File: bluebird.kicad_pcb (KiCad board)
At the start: 2 copper layers, 310.8 x 120.3 mm, 168 parts

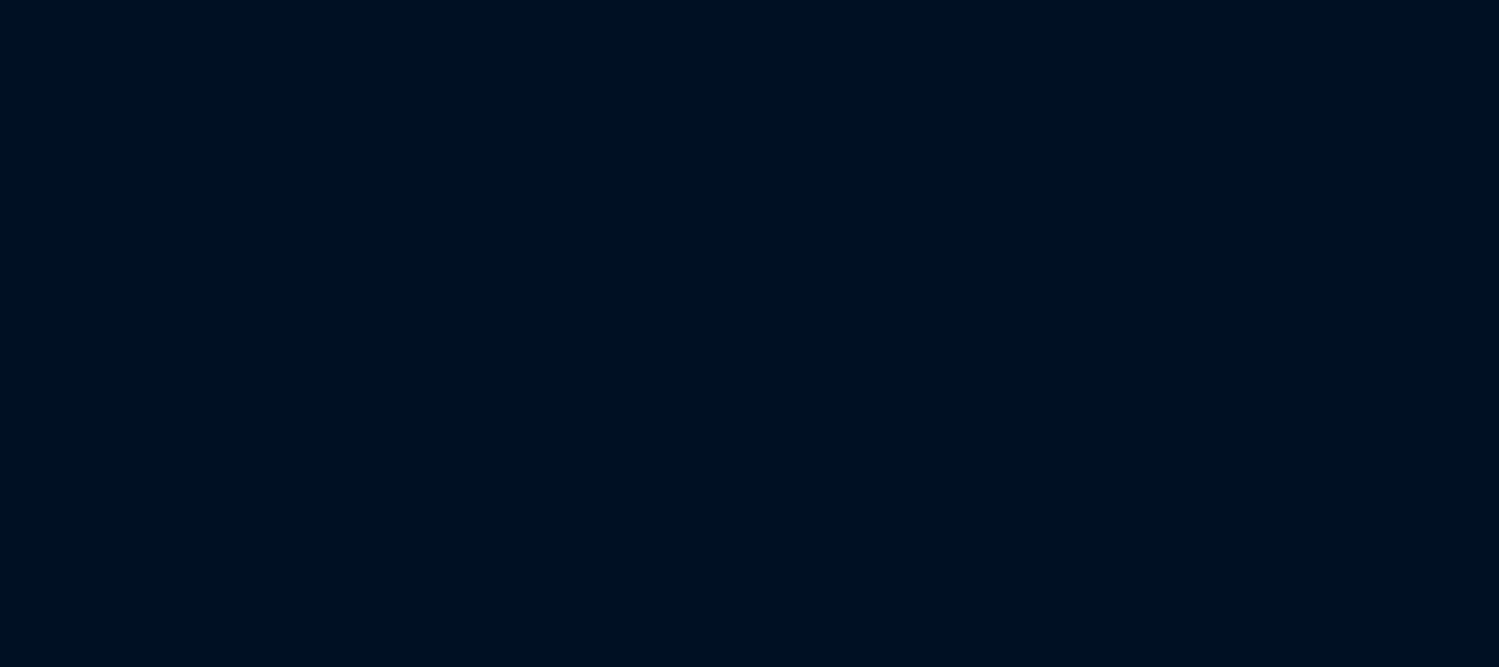
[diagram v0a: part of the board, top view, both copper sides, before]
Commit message: Add LED controller + LEDS
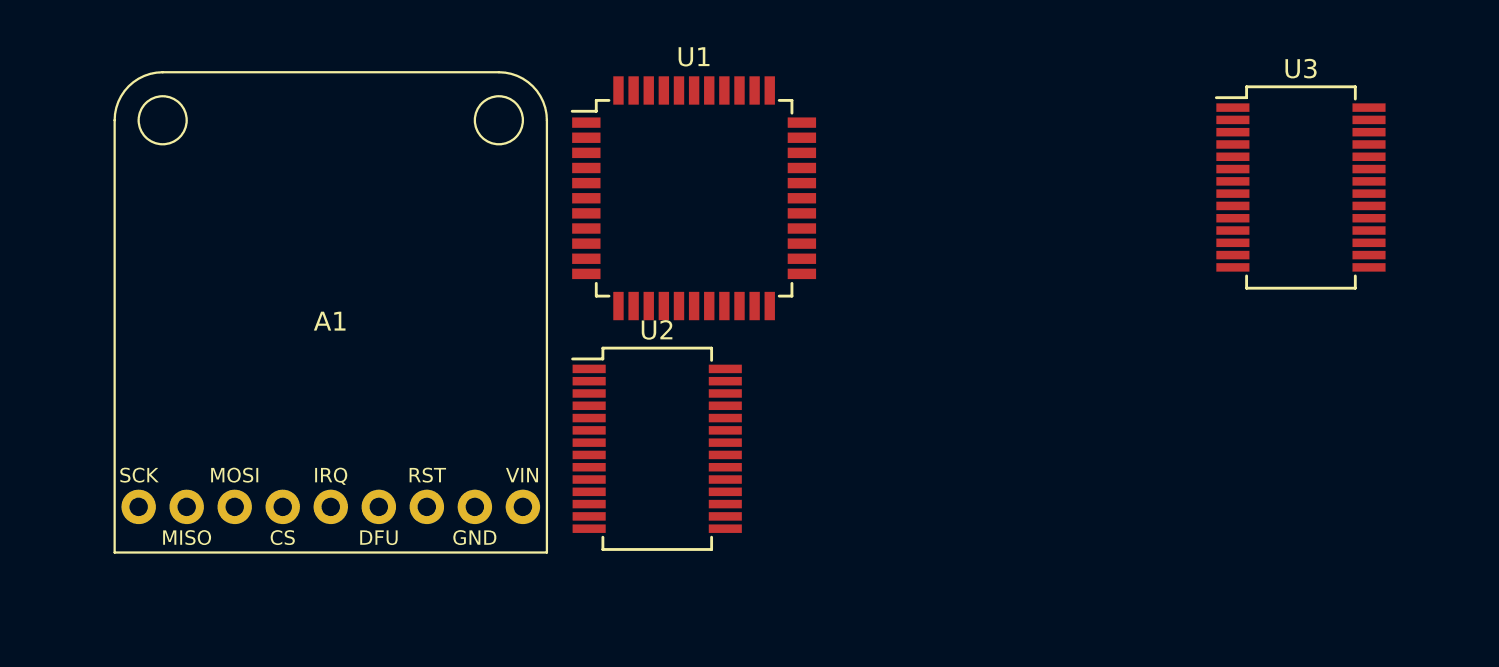
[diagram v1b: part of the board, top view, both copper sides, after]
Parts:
- added A1: BLUEFRUIT_SPI, bluebird:BLUEFRUIT_SPI_FRIEND, F.Cu at (179.8, 5.59)
- added U1: ATMEGA32U4, Package_QFP:TQFP-44_10x10mm_P0.8mm, F.Cu at (199.0, -13.1)
- added U2: MCP23017_SS, Package_SO:SSOP-28_5.3x10.2mm_P0.65mm, F.Cu at (197.1, 0.10)
- added U3: IS31FL3731-SA, Package_SO:SSOP-28_5.3x10.2mm_P0.65mm, F.Cu at (231.1, -13.7)
- K_0_0, K_1_0, K_2_0, K_3_0, K_4_0, K_5_0, K_6_0, K_7_0, K_8_0, K_9_0, K_ALT1_0, K_A_0, K_B_0, K_COMMA_0, K_CTRL1_0, K_C_0, K_DOT_0, K_DOWN_0, K_D_0, K_END_0, K_EQUAL_0, K_ESC_0, K_E_0, K_F10_0, K_F11_0, K_F12_0, K_F1_0, K_F2_0, K_F3_0, K_F4_0, K_F5_0, K_F6_0, K_F7_0, K_F8_0, K_F9_0, K_FN_0, K_F_0, K_G_0, K_HOME_0, K_H_0, K_INSERT_0, K_I_0, K_J_0, K_K_0, K_LEFT_0, K_L_0, K_MINUS_0, K_M_0, K_NMLK_0, K_N_0, K_O_0, K_PAGE_DOWN_0, K_PAGE_UP_0, K_P_0, K_QUOTE_0, K_Q_0, K_RIGHT_0, K_R_0, K_SCRLK_0, K_SEMIC_0, K_SLASH_0, K_S_0, K_T_0, K_UP_0, K_U_0, K_V_0, K_W_0, K_X_0, K_Y_0, K_Z_0, K_[_0, K_]_0, K_`_0: footprint MX_Alps_Hybrid:MX-1U-NoLED -> MX_Alps_Hybrid:MX-1U
- K_ALT_0, K_CTRL_0, K_WIN_0: footprint MX_Alps_Hybrid:MX-1.25U-NoLED -> MX_Alps_Hybrid:MX-1.25U
- K_BACKSPACE_0: footprint MX_Alps_Hybrid:MX-2U-NoLED -> MX_Alps_Hybrid:MX-2U
- K_BSLSH_0, K_TAB_0: footprint MX_Alps_Hybrid:MX-1.5U-NoLED -> MX_Alps_Hybrid:MX-1.5U
- K_CAPS_LOCK_0, K_SHIFT1_0: footprint MX_Alps_Hybrid:MX-1.75U-NoLED -> MX_Alps_Hybrid:MX-1.75U
- K_ENTER_0, K_SHIFT_0: footprint MX_Alps_Hybrid:MX-2.25U-NoLED -> MX_Alps_Hybrid:MX-2.25U
- K_SPC_0: footprint MX_Alps_Hybrid:MX-6.25U-NoLED -> MX_Alps_Hybrid:MX-6.25U
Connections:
- K_0_0 pad 3: (no net) -> Net-(K_0_0-Pad3)
- K_0_0 pad 4: (no net) -> Net-(K_0_0-Pad4)
- K_1_0 pad 3: (no net) -> Net-(K_1_0-Pad3)
- K_1_0 pad 4: (no net) -> Net-(K_1_0-Pad4)
- K_2_0 pad 3: (no net) -> Net-(K_2_0-Pad3)
- K_2_0 pad 4: (no net) -> Net-(K_2_0-Pad4)
- K_3_0 pad 3: (no net) -> Net-(K_3_0-Pad3)
- K_3_0 pad 4: (no net) -> Net-(K_3_0-Pad4)
- K_4_0 pad 3: (no net) -> Net-(K_4_0-Pad3)
- K_4_0 pad 4: (no net) -> Net-(K_4_0-Pad4)
- K_5_0 pad 3: (no net) -> Net-(K_5_0-Pad3)
- K_5_0 pad 4: (no net) -> Net-(K_5_0-Pad4)
- K_6_0 pad 3: (no net) -> Net-(K_6_0-Pad3)
- K_6_0 pad 4: (no net) -> Net-(K_6_0-Pad4)
- K_7_0 pad 3: (no net) -> Net-(K_7_0-Pad3)
- K_7_0 pad 4: (no net) -> Net-(K_7_0-Pad4)
- K_8_0 pad 3: (no net) -> Net-(K_8_0-Pad3)
- K_8_0 pad 4: (no net) -> Net-(K_8_0-Pad4)
- K_9_0 pad 3: (no net) -> Net-(K_9_0-Pad3)
- K_9_0 pad 4: (no net) -> Net-(K_9_0-Pad4)
- K_ALT1_0 pad 3: (no net) -> Net-(K_ALT1_0-Pad3)
- K_ALT1_0 pad 4: (no net) -> Net-(K_ALT1_0-Pad4)
- K_ALT_0 pad 3: (no net) -> Net-(K_ALT_0-Pad3)
- K_ALT_0 pad 4: (no net) -> Net-(K_ALT_0-Pad4)
- K_A_0 pad 3: (no net) -> Net-(K_A_0-Pad3)
- K_A_0 pad 4: (no net) -> Net-(K_A_0-Pad4)
- K_BACKSPACE_0 pad 3: (no net) -> Net-(K_BACKSPACE_0-Pad3)
- K_BACKSPACE_0 pad 4: (no net) -> Net-(K_BACKSPACE_0-Pad4)
- K_BSLSH_0 pad 3: (no net) -> Net-(K_BSLSH_0-Pad3)
- K_BSLSH_0 pad 4: (no net) -> Net-(K_BSLSH_0-Pad4)
- K_B_0 pad 3: (no net) -> Net-(K_B_0-Pad3)
- K_B_0 pad 4: (no net) -> Net-(K_B_0-Pad4)
- K_CAPS_LOCK_0 pad 3: (no net) -> Net-(K_CAPS_LOCK_0-Pad3)
- K_CAPS_LOCK_0 pad 4: (no net) -> Net-(K_CAPS_LOCK_0-Pad4)
- K_COMMA_0 pad 3: (no net) -> Net-(K_COMMA_0-Pad3)
- K_COMMA_0 pad 4: (no net) -> Net-(K_COMMA_0-Pad4)
- K_CTRL1_0 pad 3: (no net) -> Net-(K_CTRL1_0-Pad3)
- K_CTRL1_0 pad 4: (no net) -> Net-(K_CTRL1_0-Pad4)
- K_CTRL_0 pad 3: (no net) -> Net-(K_CTRL_0-Pad3)
- K_CTRL_0 pad 4: (no net) -> Net-(K_CTRL_0-Pad4)
- K_C_0 pad 3: (no net) -> Net-(K_C_0-Pad3)
- K_C_0 pad 4: (no net) -> Net-(K_C_0-Pad4)
- K_DOT_0 pad 3: (no net) -> Net-(K_DOT_0-Pad3)
- K_DOT_0 pad 4: (no net) -> Net-(K_DOT_0-Pad4)
- K_DOWN_0 pad 3: (no net) -> Net-(K_DOWN_0-Pad3)
- K_DOWN_0 pad 4: (no net) -> Net-(K_DOWN_0-Pad4)
- K_D_0 pad 3: (no net) -> Net-(K_D_0-Pad3)
- K_D_0 pad 4: (no net) -> Net-(K_D_0-Pad4)
- K_END_0 pad 3: (no net) -> Net-(K_END_0-Pad3)
- K_END_0 pad 4: (no net) -> Net-(K_END_0-Pad4)
- K_ENTER_0 pad 3: (no net) -> Net-(K_ENTER_0-Pad3)
- K_ENTER_0 pad 4: (no net) -> Net-(K_ENTER_0-Pad4)
- K_EQUAL_0 pad 3: (no net) -> Net-(K_EQUAL_0-Pad3)
- K_EQUAL_0 pad 4: (no net) -> Net-(K_EQUAL_0-Pad4)
- K_ESC_0 pad 3: (no net) -> Net-(K_ESC_0-Pad3)
- K_ESC_0 pad 4: (no net) -> Net-(K_ESC_0-Pad4)
- K_E_0 pad 3: (no net) -> Net-(K_E_0-Pad3)
- K_E_0 pad 4: (no net) -> Net-(K_E_0-Pad4)
- K_F10_0 pad 3: (no net) -> Net-(K_F10_0-Pad3)
- K_F10_0 pad 4: (no net) -> Net-(K_F10_0-Pad4)
- K_F11_0 pad 3: (no net) -> Net-(K_F11_0-Pad3)
- K_F11_0 pad 4: (no net) -> Net-(K_F11_0-Pad4)
- K_F12_0 pad 3: (no net) -> Net-(K_F12_0-Pad3)
- K_F12_0 pad 4: (no net) -> Net-(K_F12_0-Pad4)
- K_F1_0 pad 3: (no net) -> Net-(K_F1_0-Pad3)
- K_F1_0 pad 4: (no net) -> Net-(K_F1_0-Pad4)
- K_F2_0 pad 3: (no net) -> Net-(K_F2_0-Pad3)
- K_F2_0 pad 4: (no net) -> Net-(K_F2_0-Pad4)
- K_F3_0 pad 3: (no net) -> Net-(K_F3_0-Pad3)
- K_F3_0 pad 4: (no net) -> Net-(K_F3_0-Pad4)
- K_F4_0 pad 3: (no net) -> Net-(K_F4_0-Pad3)
- K_F4_0 pad 4: (no net) -> Net-(K_F4_0-Pad4)
- K_F5_0 pad 3: (no net) -> Net-(K_F5_0-Pad3)
- K_F5_0 pad 4: (no net) -> Net-(K_F5_0-Pad4)
- K_F6_0 pad 3: (no net) -> Net-(K_F6_0-Pad3)
- K_F6_0 pad 4: (no net) -> Net-(K_F6_0-Pad4)
- K_F7_0 pad 3: (no net) -> Net-(K_F7_0-Pad3)
- K_F7_0 pad 4: (no net) -> Net-(K_F7_0-Pad4)
- K_F8_0 pad 3: (no net) -> Net-(K_F8_0-Pad3)
- K_F8_0 pad 4: (no net) -> Net-(K_F8_0-Pad4)
- K_F9_0 pad 3: (no net) -> Net-(K_F9_0-Pad3)
- K_F9_0 pad 4: (no net) -> Net-(K_F9_0-Pad4)
- K_FN_0 pad 3: (no net) -> Net-(K_FN_0-Pad3)
- K_FN_0 pad 4: (no net) -> Net-(K_FN_0-Pad4)
- K_F_0 pad 3: (no net) -> Net-(K_F_0-Pad3)
- K_F_0 pad 4: (no net) -> Net-(K_F_0-Pad4)
- K_G_0 pad 3: (no net) -> Net-(K_G_0-Pad3)
- K_G_0 pad 4: (no net) -> Net-(K_G_0-Pad4)
- K_HOME_0 pad 3: (no net) -> Net-(K_HOME_0-Pad3)
- K_HOME_0 pad 4: (no net) -> Net-(K_HOME_0-Pad4)
- K_H_0 pad 3: (no net) -> Net-(K_H_0-Pad3)
- K_H_0 pad 4: (no net) -> Net-(K_H_0-Pad4)
- K_INSERT_0 pad 3: (no net) -> Net-(K_INSERT_0-Pad3)
- K_INSERT_0 pad 4: (no net) -> Net-(K_INSERT_0-Pad4)
- K_I_0 pad 3: (no net) -> Net-(K_I_0-Pad3)
- K_I_0 pad 4: (no net) -> Net-(K_I_0-Pad4)
- K_J_0 pad 3: (no net) -> Net-(K_J_0-Pad3)
- K_J_0 pad 4: (no net) -> Net-(K_J_0-Pad4)
- K_K_0 pad 3: (no net) -> Net-(K_K_0-Pad3)
- K_K_0 pad 4: (no net) -> Net-(K_K_0-Pad4)
- K_LEFT_0 pad 3: (no net) -> Net-(K_LEFT_0-Pad3)
- K_LEFT_0 pad 4: (no net) -> Net-(K_LEFT_0-Pad4)
- K_L_0 pad 3: (no net) -> Net-(K_L_0-Pad3)
- K_L_0 pad 4: (no net) -> Net-(K_L_0-Pad4)
- K_MINUS_0 pad 3: (no net) -> Net-(K_MINUS_0-Pad3)
- K_MINUS_0 pad 4: (no net) -> Net-(K_MINUS_0-Pad4)
- K_M_0 pad 3: (no net) -> Net-(K_M_0-Pad3)
- K_M_0 pad 4: (no net) -> Net-(K_M_0-Pad4)
- K_NMLK_0 pad 3: (no net) -> Net-(K_NMLK_0-Pad3)
- K_NMLK_0 pad 4: (no net) -> Net-(K_NMLK_0-Pad4)
- K_N_0 pad 3: (no net) -> Net-(K_N_0-Pad3)
- K_N_0 pad 4: (no net) -> Net-(K_N_0-Pad4)
- K_O_0 pad 3: (no net) -> Net-(K_O_0-Pad3)
- K_O_0 pad 4: (no net) -> Net-(K_O_0-Pad4)
- K_PAGE_DOWN_0 pad 3: (no net) -> Net-(K_PAGE_DOWN_0-Pad3)
- K_PAGE_DOWN_0 pad 4: (no net) -> Net-(K_PAGE_DOWN_0-Pad4)
- K_PAGE_UP_0 pad 3: (no net) -> Net-(K_PAGE_UP_0-Pad3)
- K_PAGE_UP_0 pad 4: (no net) -> Net-(K_PAGE_UP_0-Pad4)
- K_P_0 pad 3: (no net) -> Net-(K_P_0-Pad3)
- K_P_0 pad 4: (no net) -> Net-(K_P_0-Pad4)
- K_QUOTE_0 pad 3: (no net) -> Net-(K_QUOTE_0-Pad3)
- K_QUOTE_0 pad 4: (no net) -> Net-(K_QUOTE_0-Pad4)
- K_Q_0 pad 3: (no net) -> Net-(K_Q_0-Pad3)
- K_Q_0 pad 4: (no net) -> Net-(K_Q_0-Pad4)
- K_RIGHT_0 pad 3: (no net) -> Net-(K_RIGHT_0-Pad3)
- K_RIGHT_0 pad 4: (no net) -> Net-(K_RIGHT_0-Pad4)
- K_R_0 pad 3: (no net) -> Net-(K_R_0-Pad3)
- K_R_0 pad 4: (no net) -> Net-(K_R_0-Pad4)
- K_SCRLK_0 pad 3: (no net) -> Net-(K_SCRLK_0-Pad3)
- K_SCRLK_0 pad 4: (no net) -> Net-(K_SCRLK_0-Pad4)
- K_SEMIC_0 pad 3: (no net) -> Net-(K_SEMIC_0-Pad3)
- K_SEMIC_0 pad 4: (no net) -> Net-(K_SEMIC_0-Pad4)
- K_SHIFT1_0 pad 3: (no net) -> Net-(K_SHIFT1_0-Pad3)
- K_SHIFT1_0 pad 4: (no net) -> Net-(K_SHIFT1_0-Pad4)
- K_SHIFT_0 pad 3: (no net) -> Net-(K_SHIFT_0-Pad3)
- K_SHIFT_0 pad 4: (no net) -> Net-(K_SHIFT_0-Pad4)
- K_SLASH_0 pad 3: (no net) -> Net-(K_SLASH_0-Pad3)
- K_SLASH_0 pad 4: (no net) -> Net-(K_SLASH_0-Pad4)
- K_SPC_0 pad 3: (no net) -> Net-(K_SPC_0-Pad3)
- K_SPC_0 pad 4: (no net) -> Net-(K_SPC_0-Pad4)
- K_S_0 pad 3: (no net) -> Net-(K_S_0-Pad3)
- K_S_0 pad 4: (no net) -> Net-(K_S_0-Pad4)
- K_TAB_0 pad 3: (no net) -> Net-(K_TAB_0-Pad3)
- K_TAB_0 pad 4: (no net) -> Net-(K_TAB_0-Pad4)
- K_T_0 pad 3: (no net) -> Net-(K_T_0-Pad3)
- K_T_0 pad 4: (no net) -> Net-(K_T_0-Pad4)
- K_UP_0 pad 3: (no net) -> Net-(K_UP_0-Pad3)
- K_UP_0 pad 4: (no net) -> Net-(K_UP_0-Pad4)
- K_U_0 pad 3: (no net) -> Net-(K_U_0-Pad3)
- K_U_0 pad 4: (no net) -> Net-(K_U_0-Pad4)
- K_V_0 pad 3: (no net) -> Net-(K_V_0-Pad3)
- K_V_0 pad 4: (no net) -> Net-(K_V_0-Pad4)
- K_WIN_0 pad 3: (no net) -> Net-(K_WIN_0-Pad3)
- K_WIN_0 pad 4: (no net) -> Net-(K_WIN_0-Pad4)
- K_W_0 pad 3: (no net) -> Net-(K_W_0-Pad3)
- K_W_0 pad 4: (no net) -> Net-(K_W_0-Pad4)
- K_X_0 pad 3: (no net) -> Net-(K_X_0-Pad3)
- K_X_0 pad 4: (no net) -> Net-(K_X_0-Pad4)
- K_Y_0 pad 3: (no net) -> Net-(K_Y_0-Pad3)
- K_Y_0 pad 4: (no net) -> Net-(K_Y_0-Pad4)
- K_Z_0 pad 3: (no net) -> Net-(K_Z_0-Pad3)
- K_Z_0 pad 4: (no net) -> Net-(K_Z_0-Pad4)
- K_[_0 pad 3: (no net) -> Net-(K_[_0-Pad3)
- K_[_0 pad 4: (no net) -> Net-(K_[_0-Pad4)
- K_]_0 pad 3: (no net) -> Net-(K_]_0-Pad3)
- K_]_0 pad 4: (no net) -> Net-(K_]_0-Pad4)
- K_`_0 pad 3: (no net) -> Net-(K_`_0-Pad3)
- K_`_0 pad 4: (no net) -> Net-(K_`_0-Pad4)

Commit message: Finish charge controller, finish layout
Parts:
- added C1: 0.1u, Capacitor_SMD:C_0805_2012Metric_Pad1.15x1.40mm_HandSolder, B.Cu at (199.1, 144.1)
- added C10: 0.1u, Capacitor_SMD:C_0805_2012Metric_Pad1.15x1.40mm_HandSolder, B.Cu at (180.0, 136.6)
- added C11: 1u, Capacitor_SMD:C_0805_2012Metric_Pad1.15x1.40mm_HandSolder, B.Cu at (171.3, 147.7)
- added C12: 0.1u, Capacitor_SMD:C_0805_2012Metric_Pad1.15x1.40mm_HandSolder, B.Cu at (171.3, 149.7)
- added C13: 22uF, Capacitor_SMD:C_0805_2012Metric_Pad1.15x1.40mm_HandSolder, B.Cu at (132.6, 33.3)
- added C14: 22uF, Capacitor_SMD:C_0805_2012Metric_Pad1.15x1.40mm_HandSolder, B.Cu at (130.6, 33.3)
- added C15: 4.7u, Capacitor_SMD:C_0805_2012Metric_Pad1.15x1.40mm_HandSolder, B.Cu at (94.4, 34.4)
- added C2: 0.1u, Capacitor_SMD:C_0805_2012Metric_Pad1.15x1.40mm_HandSolder, B.Cu at (182.1, 141.9)
- added C3: 0.1u, Capacitor_SMD:C_0805_2012Metric_Pad1.15x1.40mm_HandSolder, B.Cu at (186.3, 130.2)
- added C4: 0.1u, Capacitor_SMD:C_0805_2012Metric_Pad1.15x1.40mm_HandSolder, B.Cu at (200.0, 134.6)
- added C5: 4.7u, Capacitor_SMD:C_0805_2012Metric_Pad1.15x1.40mm_HandSolder, B.Cu at (195.3, 147.0)
- added C6: 22p, Capacitor_SMD:C_0805_2012Metric_Pad1.15x1.40mm_HandSolder, B.Cu at (204.7, 146.2)
- added C7: 22p, Capacitor_SMD:C_0805_2012Metric_Pad1.15x1.40mm_HandSolder, B.Cu at (204.2, 136.0)
- added C8: 1u, Capacitor_SMD:C_0805_2012Metric_Pad1.15x1.40mm_HandSolder, B.Cu at (190.5, 146.9)
- added C9: 0.22u, Capacitor_SMD:C_0805_2012Metric_Pad1.15x1.40mm_HandSolder, B.Cu at (166.4, 144.2)
- added D1: B340, Diode_SMD:D_SMC, B.Cu at (163.5, 31.1)
- added D2: B340, Diode_SMD:D_SMC, B.Cu at (152.4, 31.1)
- added D3: LED_BLUE, LED_SMD:LED_0805_2012Metric, B.Cu at (97.5, 28.6)
- added D4: LED_RED, LED_SMD:LED_0805_2012Metric, B.Cu at (140.8, 31.4)
- added J1: USB_C_Receptacle_USB2.0, Connector_USB:USB_C_Receptacle_GCT_USB4085, B.Cu at (46.7, 32.4)
- added J2: Conn_01x02_Male, Connector_JST:JST_PH_S2B-PH-K_1x02_P2.00mm_Horizontal, B.Cu at (104.6, 30.9)
- added J3: Conn_01x07, Connector_PinHeader_2.54mm:PinHeader_1x07_P2.54mm_Vertical, B.Cu at (148.0, 148.0)
- added JP1: SolderJumper_3_Bridged12, Connector_PinHeader_2.54mm:PinHeader_1x03_P2.54mm_Vertical, B.Cu at (90.1, 30.9)
- added L1: 2.2u 3A, Inductor_SMD:L_Vishay_IHLP-1212, B.Cu at (118.3, 33.1)
- added R1: 10k, Resistor_SMD:R_0805_2012Metric_Pad1.15x1.40mm_HandSolder, B.Cu at (197.8, 150.1)
- added R10: 750k, Resistor_SMD:R_0805_2012Metric_Pad1.15x1.40mm_HandSolder, B.Cu at (134.7, 31.3)
- added R11: 100k, Resistor_SMD:R_0805_2012Metric_Pad1.15x1.40mm_HandSolder, B.Cu at (137.6, 30.3)
- added R12: 1k, Resistor_SMD:R_0805_2012Metric_Pad1.15x1.40mm_HandSolder, B.Cu at (99.5, 28.6)
- added R13: 2k, Resistor_SMD:R_0805_2012Metric_Pad1.15x1.40mm_HandSolder, B.Cu at (86.9, 30.1)
- added R14: 10k, Resistor_SMD:R_0805_2012Metric_Pad1.15x1.40mm_HandSolder, B.Cu at (86.9, 32.2)
- added R15: 4.7k, Resistor_SMD:R_0805_2012Metric_Pad1.15x1.40mm_HandSolder, B.Cu at (143.8, 30.3)
- added R2: 22R, Resistor_SMD:R_0805_2012Metric_Pad1.15x1.40mm_HandSolder, B.Cu at (190.5, 151.1)
- added R3: 22R, Resistor_SMD:R_0805_2012Metric_Pad1.15x1.40mm_HandSolder, B.Cu at (190.6, 149.0)
- added R4: 10k, Resistor_SMD:R_0805_2012Metric_Pad1.15x1.40mm_HandSolder, B.Cu at (197.4, 132.0)
- added R5: 10k, Resistor_SMD:R_0805_2012Metric_Pad1.15x1.40mm_HandSolder, B.Cu at (123.7, 138.5)
- added R6: 10k, Resistor_SMD:R_0805_2012Metric_Pad1.15x1.40mm_HandSolder, B.Cu at (125.9, 138.5)
- added R7: 20k, Resistor_SMD:R_0805_2012Metric_Pad1.15x1.40mm_HandSolder, B.Cu at (175.2, 147.8)
- added R8: 10k, Resistor_SMD:R_0805_2012Metric_Pad1.15x1.40mm_HandSolder, B.Cu at (121.2, 32.0)
- added R9: DNP, Resistor_SMD:R_0805_2012Metric_Pad1.15x1.40mm_HandSolder, B.Cu at (137.2, 34.2)
- added S1: EG2219, bluebird:SW_EG2219, B.Cu at (76.2, 31.4)
- added SW1: SW_PUSH, Button_Switch_SMD:SW_SPST_TL3342, B.Cu at (212.9, 141.0)
- added U4: PAM2401, Silicon-Standard:MSOP8, B.Cu at (126.3, 32.4)
- added U5: MCP73831-2-OT, Package_TO_SOT_SMD:SOT-23-5, B.Cu at (98.5, 32.3)
- added Y1: FA328 16MHz, Crystal:Crystal_SMD_SeikoEpson_FA238-4Pin_3.2x2.5mm_HandSoldering, B.Cu at (203.4, 140.9)
- A1, U1, U2, U3: moved to B.Cu
- moved U2 165.2 mm to (121.8, 147.2), turned to 270 degrees
- moved U3 164.9 mm to (174.1, 141.1)
- moved U1 151.8 mm to (190.9, 138.5), turned to 90 degrees
- moved A1 140.9 mm to (125.5, 135.5), turned to 180 degrees
- moved D_BACKSPACE_0 17.6 mm to (276.3, 64.7)
- moved D_LEFT_0 17.6 mm to (276.3, 140.9)
- moved D_NMLK_0 17.6 mm to (276.3, 45.7)
- moved K_BSLSH_0 17.6 mm to (299.6, 83.3)
- moved K_END_0 17.6 mm to (323.4, 121.4)
- moved K_HOME_0 17.6 mm to (323.4, 64.2)
- moved K_INSERT_0 17.6 mm to (323.4, 45.2)
- moved K_PAGE_DOWN_0 17.6 mm to (323.4, 102.3)
- moved K_PAGE_UP_0 17.6 mm to (323.4, 83.3)
- moved K_RIGHT_0 17.6 mm to (323.4, 140.4)
- moved K_]_0 17.6 mm to (275.8, 83.3)
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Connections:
- K_0_0 pad 3: Net-(K_0_0-Pad3) -> LED_CB4
- K_0_0 pad 4: Net-(K_0_0-Pad4) -> LED_CB2
- K_1_0 pad 3: Net-(K_1_0-Pad3) -> LED_CA3
- K_1_0 pad 4: Net-(K_1_0-Pad4) -> LED_CA2
- K_2_0 pad 3: Net-(K_2_0-Pad3) -> LED_CA4
- K_2_0 pad 4: Net-(K_2_0-Pad4) -> LED_CA2
- K_3_0 pad 3: Net-(K_3_0-Pad3) -> LED_CA5
- K_3_0 pad 4: Net-(K_3_0-Pad4) -> LED_CA2
- K_4_0 pad 3: Net-(K_4_0-Pad3) -> LED_CA6
- K_4_0 pad 4: Net-(K_4_0-Pad4) -> LED_CA2
- K_5_0 pad 3: Net-(K_5_0-Pad3) -> LED_CA7
- K_5_0 pad 4: Net-(K_5_0-Pad4) -> LED_CA2
- K_6_0 pad 3: Net-(K_6_0-Pad3) -> LED_CA8
- K_6_0 pad 4: Net-(K_6_0-Pad4) -> LED_CA2
- K_7_0 pad 3: Net-(K_7_0-Pad3) -> LED_CA9
- K_7_0 pad 4: Net-(K_7_0-Pad4) -> LED_CA2
- K_8_0 pad 3: Net-(K_8_0-Pad3) -> LED_CB1
- K_8_0 pad 4: Net-(K_8_0-Pad4) -> LED_CB2
- K_9_0 pad 3: Net-(K_9_0-Pad3) -> LED_CB3
- K_9_0 pad 4: Net-(K_9_0-Pad4) -> LED_CB2
- K_ALT1_0 pad 3: Net-(K_ALT1_0-Pad3) -> LED_CA5
- K_ALT1_0 pad 4: Net-(K_ALT1_0-Pad4) -> LED_CA6
- K_ALT_0 pad 3: Net-(K_ALT_0-Pad3) -> LED_CA3
- K_ALT_0 pad 4: Net-(K_ALT_0-Pad4) -> LED_CA6
- K_A_0 pad 3: Net-(K_A_0-Pad3) -> LED_CA2
- K_A_0 pad 4: Net-(K_A_0-Pad4) -> LED_CA4
- K_BACKSPACE_0 pad 3: Net-(K_BACKSPACE_0-Pad3) -> LED_CB7
- K_BACKSPACE_0 pad 4: Net-(K_BACKSPACE_0-Pad4) -> LED_CB2
- K_BSLSH_0 pad 3: Net-(K_BSLSH_0-Pad3) -> LED_CB7
- K_BSLSH_0 pad 4: Net-(K_BSLSH_0-Pad4) -> LED_CB3
- K_B_0 pad 3: Net-(K_B_0-Pad3) -> LED_CA7
- K_B_0 pad 4: Net-(K_B_0-Pad4) -> LED_CA5
- K_CAPS_LOCK_0 pad 3: Net-(K_CAPS_LOCK_0-Pad3) -> LED_CA1
- K_CAPS_LOCK_0 pad 4: Net-(K_CAPS_LOCK_0-Pad4) -> LED_CA4
- K_COMMA_0 pad 3: Net-(K_COMMA_0-Pad3) -> LED_CB1
- K_COMMA_0 pad 4: Net-(K_COMMA_0-Pad4) -> LED_CB5
- K_CTRL1_0 pad 3: Net-(K_CTRL1_0-Pad3) -> LED_CA8
- K_CTRL1_0 pad 4: Net-(K_CTRL1_0-Pad4) -> LED_CA6
- K_CTRL_0 pad 3: Net-(K_CTRL_0-Pad3) -> LED_CA1
- K_CTRL_0 pad 4: Net-(K_CTRL_0-Pad4) -> LED_CA6
- K_C_0 pad 3: Net-(K_C_0-Pad3) -> LED_CA4
- K_C_0 pad 4: Net-(K_C_0-Pad4) -> LED_CA5
- K_DOT_0 pad 3: Net-(K_DOT_0-Pad3) -> LED_CB2
- K_DOT_0 pad 4: Net-(K_DOT_0-Pad4) -> LED_CB5
- K_DOWN_0 pad 3: Net-(K_DOWN_0-Pad3) -> LED_CB1
- K_DOWN_0 pad 4: Net-(K_DOWN_0-Pad4) -> LED_CB6
- K_D_0 pad 3: Net-(K_D_0-Pad3) -> LED_CA5
- K_D_0 pad 4: Net-(K_D_0-Pad4) -> LED_CA4
- K_END_0 pad 3: Net-(K_END_0-Pad3) -> LED_CB7
- K_END_0 pad 4: Net-(K_END_0-Pad4) -> LED_CB5
- K_ENTER_0 pad 3: Net-(K_ENTER_0-Pad3) -> LED_CB6
- K_ENTER_0 pad 4: Net-(K_ENTER_0-Pad4) -> LED_CB4
- K_EQUAL_0 pad 3: Net-(K_EQUAL_0-Pad3) -> LED_CB6
- K_EQUAL_0 pad 4: Net-(K_EQUAL_0-Pad4) -> LED_CB2
- K_ESC_0 pad 3: Net-(K_ESC_0-Pad3) -> LED_CA2
- K_ESC_0 pad 4: Net-(K_ESC_0-Pad4) -> LED_CA1
- K_E_0 pad 3: Net-(K_E_0-Pad3) -> LED_CA5
- K_E_0 pad 4: Net-(K_E_0-Pad4) -> LED_CA3
- K_F10_0 pad 3: Net-(K_F10_0-Pad3) -> LED_CB4
- K_F10_0 pad 4: Net-(K_F10_0-Pad4) -> LED_CB1
- K_F11_0 pad 3: Net-(K_F11_0-Pad3) -> LED_CB5
- K_F11_0 pad 4: Net-(K_F11_0-Pad4) -> LED_CB1
- K_F12_0 pad 3: Net-(K_F12_0-Pad3) -> LED_CB6
- K_F12_0 pad 4: Net-(K_F12_0-Pad4) -> LED_CB1
- K_F1_0 pad 3: Net-(K_F1_0-Pad3) -> LED_CA3
- K_F1_0 pad 4: Net-(K_F1_0-Pad4) -> LED_CA1
- K_F2_0 pad 3: Net-(K_F2_0-Pad3) -> LED_CA4
- K_F2_0 pad 4: Net-(K_F2_0-Pad4) -> LED_CA1
- K_F3_0 pad 3: Net-(K_F3_0-Pad3) -> LED_CA5
- K_F3_0 pad 4: Net-(K_F3_0-Pad4) -> LED_CA1
- K_F4_0 pad 3: Net-(K_F4_0-Pad3) -> LED_CA6
- K_F4_0 pad 4: Net-(K_F4_0-Pad4) -> LED_CA1
- K_F5_0 pad 3: Net-(K_F5_0-Pad3) -> LED_CA7
- K_F5_0 pad 4: Net-(K_F5_0-Pad4) -> LED_CA1
- K_F6_0 pad 3: Net-(K_F6_0-Pad3) -> LED_CA8
- K_F6_0 pad 4: Net-(K_F6_0-Pad4) -> LED_CA1
- K_F7_0 pad 3: Net-(K_F7_0-Pad3) -> LED_CA9
- K_F7_0 pad 4: Net-(K_F7_0-Pad4) -> LED_CA1
- K_F8_0 pad 3: Net-(K_F8_0-Pad3) -> LED_CB2
- K_F8_0 pad 4: Net-(K_F8_0-Pad4) -> LED_CB1
- K_F9_0 pad 3: Net-(K_F9_0-Pad3) -> LED_CB3
- K_F9_0 pad 4: Net-(K_F9_0-Pad4) -> LED_CB1
- K_FN_0 pad 3: Net-(K_FN_0-Pad3) -> LED_CA7
- K_FN_0 pad 4: Net-(K_FN_0-Pad4) -> LED_CA6
- K_F_0 pad 3: Net-(K_F_0-Pad3) -> LED_CA6
- K_F_0 pad 4: Net-(K_F_0-Pad4) -> LED_CA4
- K_G_0 pad 3: Net-(K_G_0-Pad3) -> LED_CA7
- K_G_0 pad 4: Net-(K_G_0-Pad4) -> LED_CA4
- K_HOME_0 pad 3: Net-(K_HOME_0-Pad3) -> LED_CB8
- K_HOME_0 pad 4: Net-(K_HOME_0-Pad4) -> LED_CB2
- K_H_0 pad 3: Net-(K_H_0-Pad3) -> LED_CA8
- K_H_0 pad 4: Net-(K_H_0-Pad4) -> LED_CA4
- K_INSERT_0 pad 3: Net-(K_INSERT_0-Pad3) -> LED_CB9
- K_INSERT_0 pad 4: Net-(K_INSERT_0-Pad4) -> LED_CB1
- K_I_0 pad 3: Net-(K_I_0-Pad3) -> LED_CB1
- K_I_0 pad 4: Net-(K_I_0-Pad4) -> LED_CB3
- K_J_0 pad 3: Net-(K_J_0-Pad3) -> LED_CA9
- K_J_0 pad 4: Net-(K_J_0-Pad4) -> LED_CA4
- K_K_0 pad 3: Net-(K_K_0-Pad3) -> LED_CB1
- K_K_0 pad 4: Net-(K_K_0-Pad4) -> LED_CB4
- K_LEFT_0 pad 3: Net-(K_LEFT_0-Pad3) -> LED_CA9
- K_LEFT_0 pad 4: Net-(K_LEFT_0-Pad4) -> LED_CA6
- K_L_0 pad 3: Net-(K_L_0-Pad3) -> LED_CB2
- K_L_0 pad 4: Net-(K_L_0-Pad4) -> LED_CB4
- K_MINUS_0 pad 3: Net-(K_MINUS_0-Pad3) -> LED_CB5
- K_MINUS_0 pad 4: Net-(K_MINUS_0-Pad4) -> LED_CB2
- K_M_0 pad 3: Net-(K_M_0-Pad3) -> LED_CA9
- K_M_0 pad 4: Net-(K_M_0-Pad4) -> LED_CA5
- K_NMLK_0 pad 3: Net-(K_NMLK_0-Pad3) -> LED_CB8
- K_NMLK_0 pad 4: Net-(K_NMLK_0-Pad4) -> LED_CB1
- K_N_0 pad 3: Net-(K_N_0-Pad3) -> LED_CA8
- K_N_0 pad 4: Net-(K_N_0-Pad4) -> LED_CA5
- K_O_0 pad 3: Net-(K_O_0-Pad3) -> LED_CB2
- K_O_0 pad 4: Net-(K_O_0-Pad4) -> LED_CB3
- K_PAGE_DOWN_0 pad 3: Net-(K_PAGE_DOWN_0-Pad3) -> LED_CB7
- K_PAGE_DOWN_0 pad 4: Net-(K_PAGE_DOWN_0-Pad4) -> LED_CB4
- K_PAGE_UP_0 pad 3: Net-(K_PAGE_UP_0-Pad3) -> LED_CB8
- K_PAGE_UP_0 pad 4: Net-(K_PAGE_UP_0-Pad4) -> LED_CB3
- K_P_0 pad 3: Net-(K_P_0-Pad3) -> LED_CB4
- K_P_0 pad 4: Net-(K_P_0-Pad4) -> LED_CB3
- K_QUOTE_0 pad 3: Net-(K_QUOTE_0-Pad3) -> LED_CB5
- K_QUOTE_0 pad 4: Net-(K_QUOTE_0-Pad4) -> LED_CB4
- K_Q_0 pad 3: Net-(K_Q_0-Pad3) -> LED_CA2
- K_Q_0 pad 4: Net-(K_Q_0-Pad4) -> LED_CA3
- K_RIGHT_0 pad 3: Net-(K_RIGHT_0-Pad3) -> LED_CB2
- K_RIGHT_0 pad 4: Net-(K_RIGHT_0-Pad4) -> LED_CB6
- K_R_0 pad 3: Net-(K_R_0-Pad3) -> LED_CA6
- K_R_0 pad 4: Net-(K_R_0-Pad4) -> LED_CA3
- K_SCRLK_0 pad 3: Net-(K_SCRLK_0-Pad3) -> LED_CB7
- K_SCRLK_0 pad 4: Net-(K_SCRLK_0-Pad4) -> LED_CB1
- K_SEMIC_0 pad 3: Net-(K_SEMIC_0-Pad3) -> LED_CB3
- K_SEMIC_0 pad 4: Net-(K_SEMIC_0-Pad4) -> LED_CB4
- K_SHIFT1_0 pad 3: Net-(K_SHIFT1_0-Pad3) -> LED_CB4
- K_SHIFT1_0 pad 4: Net-(K_SHIFT1_0-Pad4) -> LED_CB5
- K_SHIFT_0 pad 3: Net-(K_SHIFT_0-Pad3) -> LED_CA1
- K_SHIFT_0 pad 4: Net-(K_SHIFT_0-Pad4) -> LED_CA5
- K_SLASH_0 pad 3: Net-(K_SLASH_0-Pad3) -> LED_CB3
- K_SLASH_0 pad 4: Net-(K_SLASH_0-Pad4) -> LED_CB5
- K_SPC_0 pad 3: Net-(K_SPC_0-Pad3) -> LED_CA4
- K_SPC_0 pad 4: Net-(K_SPC_0-Pad4) -> LED_CA6
- K_S_0 pad 3: Net-(K_S_0-Pad3) -> LED_CA3
- K_S_0 pad 4: Net-(K_S_0-Pad4) -> LED_CA4
- K_TAB_0 pad 3: Net-(K_TAB_0-Pad3) -> LED_CA1
- K_TAB_0 pad 4: Net-(K_TAB_0-Pad4) -> LED_CA3
- K_T_0 pad 3: Net-(K_T_0-Pad3) -> LED_CA7
- K_T_0 pad 4: Net-(K_T_0-Pad4) -> LED_CA3
- K_UP_0 pad 3: Net-(K_UP_0-Pad3) -> LED_CB6
- K_UP_0 pad 4: Net-(K_UP_0-Pad4) -> LED_CB5
- K_U_0 pad 3: Net-(K_U_0-Pad3) -> LED_CA9
- K_U_0 pad 4: Net-(K_U_0-Pad4) -> LED_CA3
- K_V_0 pad 3: Net-(K_V_0-Pad3) -> LED_CA6
- K_V_0 pad 4: Net-(K_V_0-Pad4) -> LED_CA5
- K_WIN_0 pad 3: Net-(K_WIN_0-Pad3) -> LED_CA2
- K_WIN_0 pad 4: Net-(K_WIN_0-Pad4) -> LED_CA6
- K_W_0 pad 3: Net-(K_W_0-Pad3) -> LED_CA4
- K_W_0 pad 4: Net-(K_W_0-Pad4) -> LED_CA3
- K_X_0 pad 3: Net-(K_X_0-Pad3) -> LED_CA3
- K_X_0 pad 4: Net-(K_X_0-Pad4) -> LED_CA5
- K_Y_0 pad 3: Net-(K_Y_0-Pad3) -> LED_CA8
- K_Y_0 pad 4: Net-(K_Y_0-Pad4) -> LED_CA3
- K_Z_0 pad 3: Net-(K_Z_0-Pad3) -> LED_CA2
- K_Z_0 pad 4: Net-(K_Z_0-Pad4) -> LED_CA5
- K_[_0 pad 3: Net-(K_[_0-Pad3) -> LED_CB5
- K_[_0 pad 4: Net-(K_[_0-Pad4) -> LED_CB3
- K_]_0 pad 3: Net-(K_]_0-Pad3) -> LED_CB6
- K_]_0 pad 4: Net-(K_]_0-Pad4) -> LED_CB3
- K_`_0 pad 3: Net-(K_`_0-Pad3) -> LED_CA1
- K_`_0 pad 4: Net-(K_`_0-Pad4) -> LED_CA2
- U1 pad 30: Net-(U1-Pad30) -> LED_INT
- U1 pad 31: Net-(U1-Pad31) -> LED_SHDN
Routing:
- added copper zone on B.Cu, net GND
- added copper zone on F.Cu, net VCC
- removed copper zone on F.Cu, net GND
- removed copper zone on B.Cu, net VCC
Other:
- board size 310.8 x 120.3 mm -> 310.8 x 126.6 mm
- board text added: "BLE_DFU"
- board text added: "GND"
- board text added: "LED_AUD_IN"
- board text added: "VBAT"
- board text added: "VCC"
- board text added: "VCC_BAT"
- board text added: "VUSB"

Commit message: Route switches
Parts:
- J3: value Conn_01x07 -> Conn_01x05; footprint Connector_PinHeader_2.54mm:PinHeader_1x07_P2.54mm_Vertical -> Connector_PinHeader_2.54mm:PinHeader_1x05_P2.54mm_Vertical; moved to F.Cu
- JP1: footprint Connector_PinHeader_2.54mm:PinHeader_1x03_P2.54mm_Vertical -> Jumper:SolderJumper-3_P1.3mm_Bridged2Bar12_Pad1.0x1.5mm
- moved J3 122.1 mm to (183.0, 31.0), turned to 270 degrees
- moved R5 14.1 mm to (137.8, 139.2)
- moved R9 12.3 mm to (126.2, 28.6), turned to 180 degrees
- moved R6 11.0 mm to (129.3, 148.9), turned to 180 degrees
- moved C6 10.1 mm to (204.2, 136.1)
- moved C7 9.67 mm to (204.7, 145.7)
- moved U2 5.42 mm to (123.9, 142.1), turned to 180 degrees
- moved R13 2.22 mm to (88.9, 29.2)
- moved R14 2.22 mm to (88.9, 31.3)
- moved JP1 2.22 mm to (92.2, 30.0)
- moved C15 0.10 mm to (94.4, 34.3)
- turned D3 to 270 degrees
- turned R12 to 270 degrees
- turned SW1 to 90 degrees
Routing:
- net LED_CA6: track 0.00 -> 476.1 mm
- net LED_CB1: track 0.00 -> 443.7 mm, vias 0 -> 2
- net col9: track 0.00 -> 408.9 mm, vias 0 -> 1
- net col8: track 0.00 -> 393.9 mm, vias 0 -> 2
- net col12: track 0.00 -> 349.0 mm, vias 0 -> 2
- net LED_CB2: track 0.00 -> 339.7 mm, vias 0 -> 1
- net col13: track 0.00 -> 337.7 mm, vias 0 -> 1
- net col14: track 0.00 -> 330.2 mm, vias 0 -> 5
- net col15: track 0.00 -> 324.5 mm, vias 0 -> 3
- net USB_DP: track 0.00 -> 307.1 mm, vias 0 -> 2
- net LED_CA5: track 0.00 -> 302.9 mm
- net USB_DM: track 0.00 -> 302.2 mm, vias 0 -> 2
- net row0: track 0.00 -> 297.8 mm
- net col7: track 0.00 -> 297.5 mm, vias 0 -> 3
- net row2: track 0.00 -> 297.0 mm
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- added copper zone on B.Cu, net VUSB
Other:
- net class Key added: clearance 0.2, trace_width 0.6, via_dia 0.8, via_drill 0.4
- net class Power added: clearance 0.2, trace_width 0.8, via_dia 1, via_drill 0.6
- board text added: "100mA"
- board text added: "500mA"
